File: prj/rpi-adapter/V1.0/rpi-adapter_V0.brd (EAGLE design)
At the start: 67.8 x 63.5 mm, 8 parts

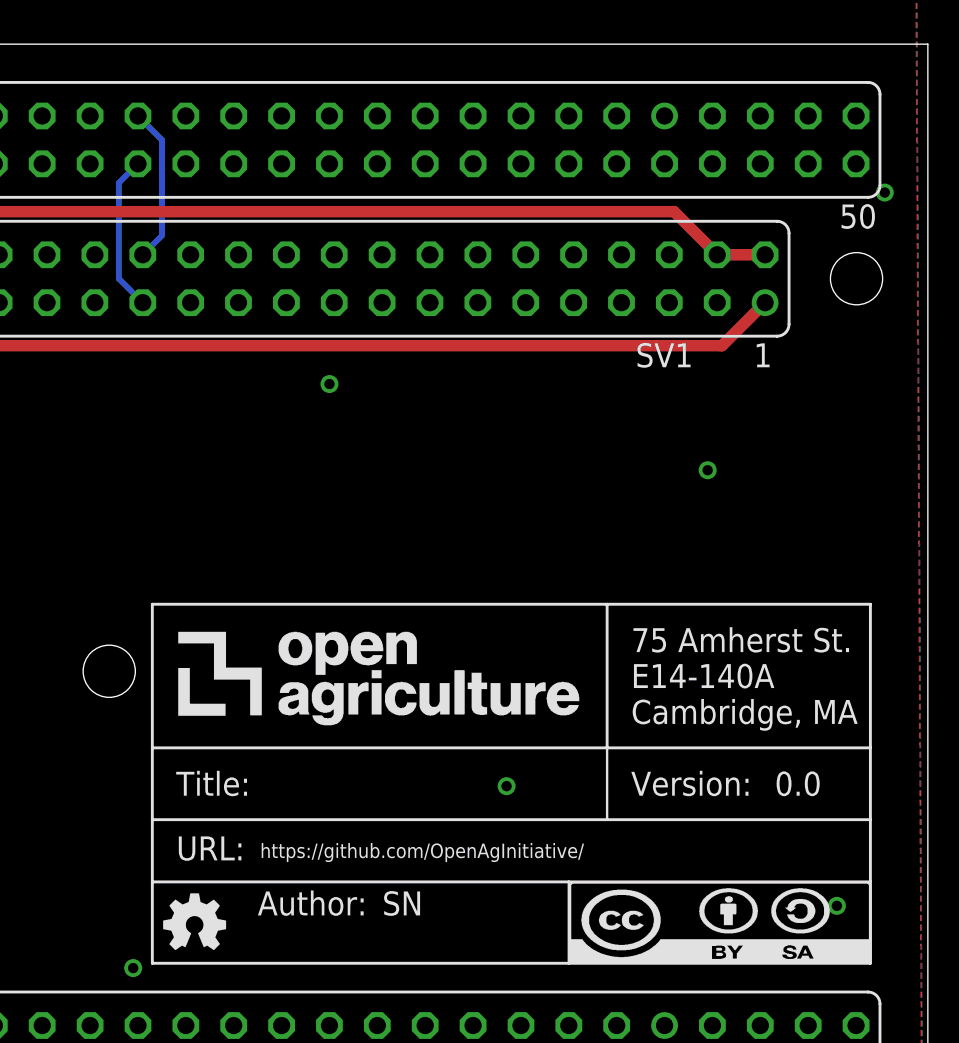
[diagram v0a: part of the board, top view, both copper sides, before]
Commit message: Added boards
waterbot board, relay board
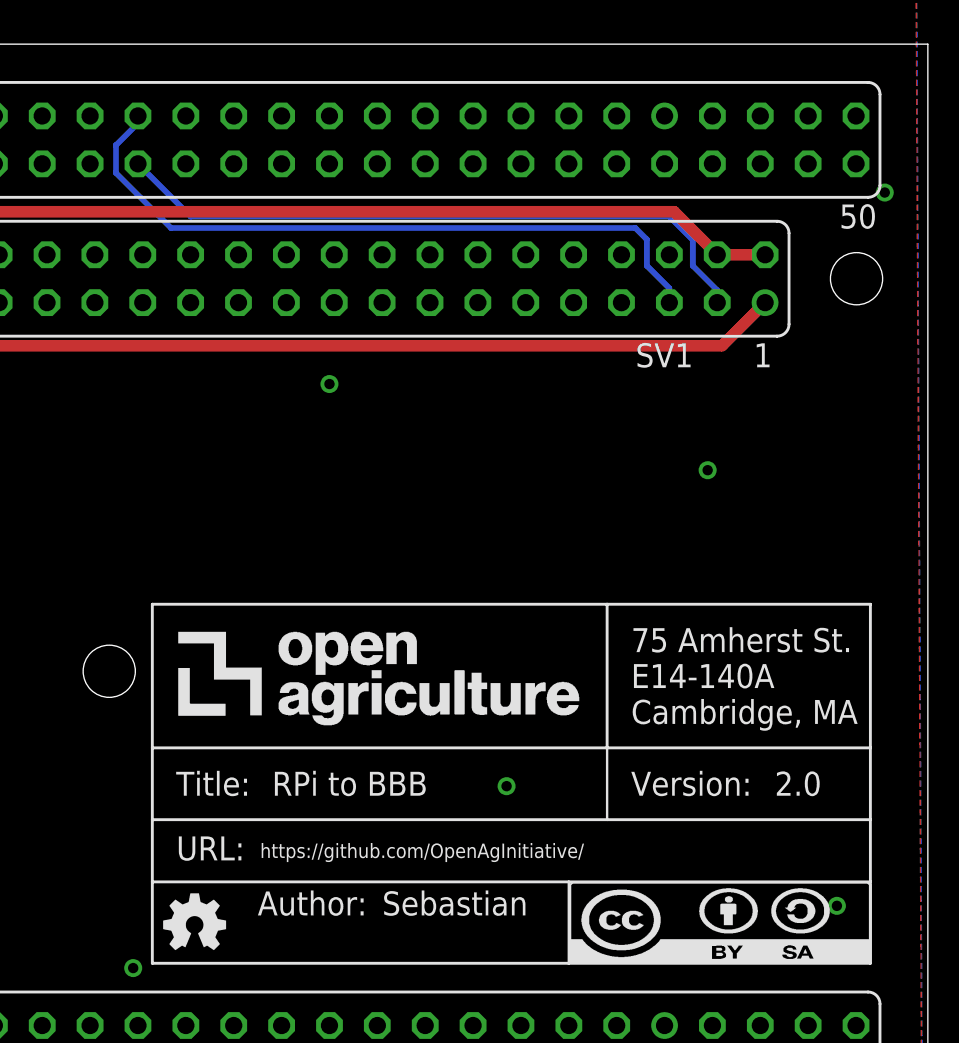
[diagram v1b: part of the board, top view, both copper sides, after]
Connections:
- net SCL: now also SV1.5; no longer SV1.28
- net SDA: now also SV1.3; no longer SV1.27
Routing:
- net SCL: track 8.31 -> 37.0 mm
- net SDA: track 8.31 -> 35.0 mm
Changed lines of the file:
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@@
 <elements>
 <element name="ATTRIBUTES" library="openag-frames" package="DOCFIELD" value="" x="47.244" y="12.7" smashed="yes">
-<attribute name="AUTHOR" value="SN" x="59.436" y="15.24" size="1.27" layer="21"/>
-<attribute name="DESCRIPTION" value="RPi to BBB adapter" x="46.228" y="12.7" size="1.778" layer="27" display="off"/>
+<attribute name="AUTHOR" value="Sebastian" x="59.436" y="15.24" size="1.27" layer="21"/>
+<attribute name="DESCRIPTION" value="RPi to BBB" x="46.228" y="12.7" size="1.778" layer="27" display="off"/>
 <attribute name="LAST_DATE_TIME" x="52.832" y="13.335" size="1.27" layer="21"/>
-<attribute name="TITLE" value="RPi adapter" x="53.594" y="21.59" size="1.27" layer="21" display="off"/>
+<attribute name="TITLE" value="RPi to BBB" x="53.594" y="21.59" size="1.27" layer="21"/>
 <attribute name="URL" value="https://github.com/OpenAgInitiative/" x="52.959" y="18.288" size="0.762" layer="21"/>
-<attribute name="VER" value="0.0" x="80.264" y="21.59" size="1.27" layer="21"/>
+<attribute name="VER" value="2.0" x="80.264" y="21.59" size="1.27" layer="21"/>
 </element>
 <element name="D2" library="openag-diodes" package="CHIPLED_0603" value="APT1608CGCK" x="24.384" y="38.608" smashed="yes" rot="R90">
@@
 </signal>
 <signal name="SDA">
-<contactref element="SV1" pad="27"/>
 <contactref element="SV2" pad="20"/>
-<wire x1="46.482" y1="55.118" x2="45.466" y2="54.102" width="0.3048" layer="16"/>
-<wire x1="45.466" y1="49.022" x2="46.736" y2="47.752" width="0.3048" layer="16"/>
-<wire x1="45.466" y1="54.102" x2="45.466" y2="49.022" width="0.3048" layer="16"/>
+<contactref element="SV1" pad="3"/>
+<wire x1="77.216" y1="47.752" x2="77.216" y2="48.41103125" width="0.3048" layer="16"/>
+<wire x1="75.9206" y1="51.0794" x2="74.676" y2="52.324" width="0.3048" layer="16"/>
+<wire x1="77.216" y1="48.41103125" x2="75.9206" y2="49.70643125" width="0.3048" layer="16"/>
+<wire x1="75.9206" y1="49.70643125" x2="75.9206" y2="51.0794" width="0.3048" layer="16"/>
+<wire x1="74.676" y1="52.324" x2="49.276" y2="52.324" width="0.3048" layer="16"/>
+<wire x1="49.276" y1="52.324" x2="46.482" y2="55.118" width="0.3048" layer="16"/>
 </signal>
 <signal name="SCL">
-<contactref element="SV1" pad="28"/>
 <contactref element="SV2" pad="19"/>
-<wire x1="46.482" y1="57.658" x2="47.752" y2="56.388" width="0.3048" layer="16"/>
-<wire x1="47.752" y1="56.388" x2="47.752" y2="51.308" width="0.3048" layer="16"/>
-<wire x1="47.752" y1="51.308" x2="46.736" y2="50.292" width="0.3048" layer="16"/>
+<contactref element="SV1" pad="5"/>
+<wire x1="45.3136" y1="56.10996875" x2="45.3136" y2="54.63403125" width="0.3048" layer="16"/>
+<wire x1="46.482" y1="57.658" x2="46.482" y2="57.27836875" width="0.3048" layer="16"/>
+<wire x1="46.482" y1="57.27836875" x2="45.3136" y2="56.10996875" width="0.3048" layer="16"/>
+<wire x1="45.3136" y1="54.63403125" x2="48.23323125" y2="51.7144" width="0.3048" layer="16"/>
+<wire x1="74.676" y1="48.514" x2="74.676" y2="47.752" width="0.3048" layer="16"/>
+<wire x1="74.676" y1="48.514" x2="73.4822" y2="49.7078" width="0.3048" layer="16"/>
+<wire x1="73.4822" y1="51.10616875" x2="73.4822" y2="49.7078" width="0.3048" layer="16"/>
+<wire x1="72.87396875" y1="51.7144" x2="73.4822" y2="51.10616875" width="0.3048" layer="16"/>
+<wire x1="48.23323125" y1="51.7144" x2="72.87396875" y2="51.7144" width="0.3048" layer="16"/>
 </signal>
 </signals>
